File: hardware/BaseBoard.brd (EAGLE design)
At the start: 71.1 x 46.8 mm, 10 parts

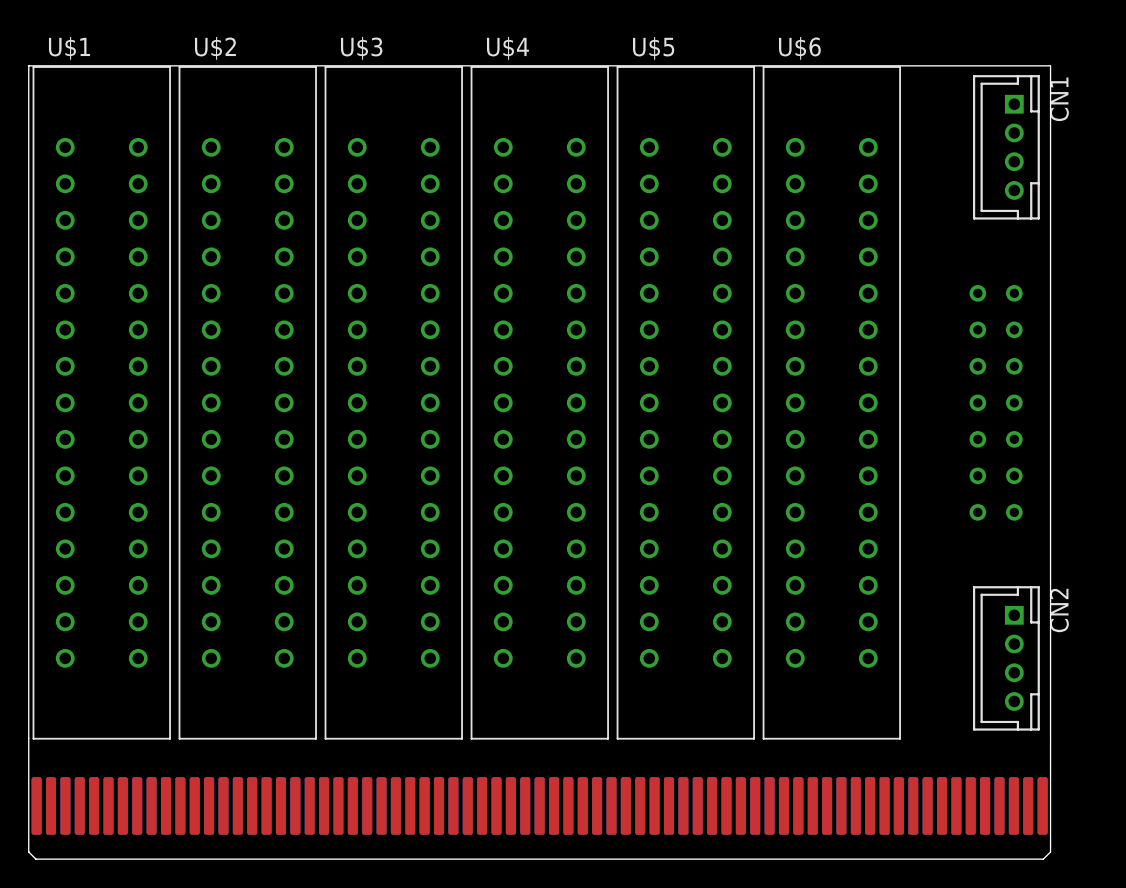
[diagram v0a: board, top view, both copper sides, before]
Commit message: Layout and route base board
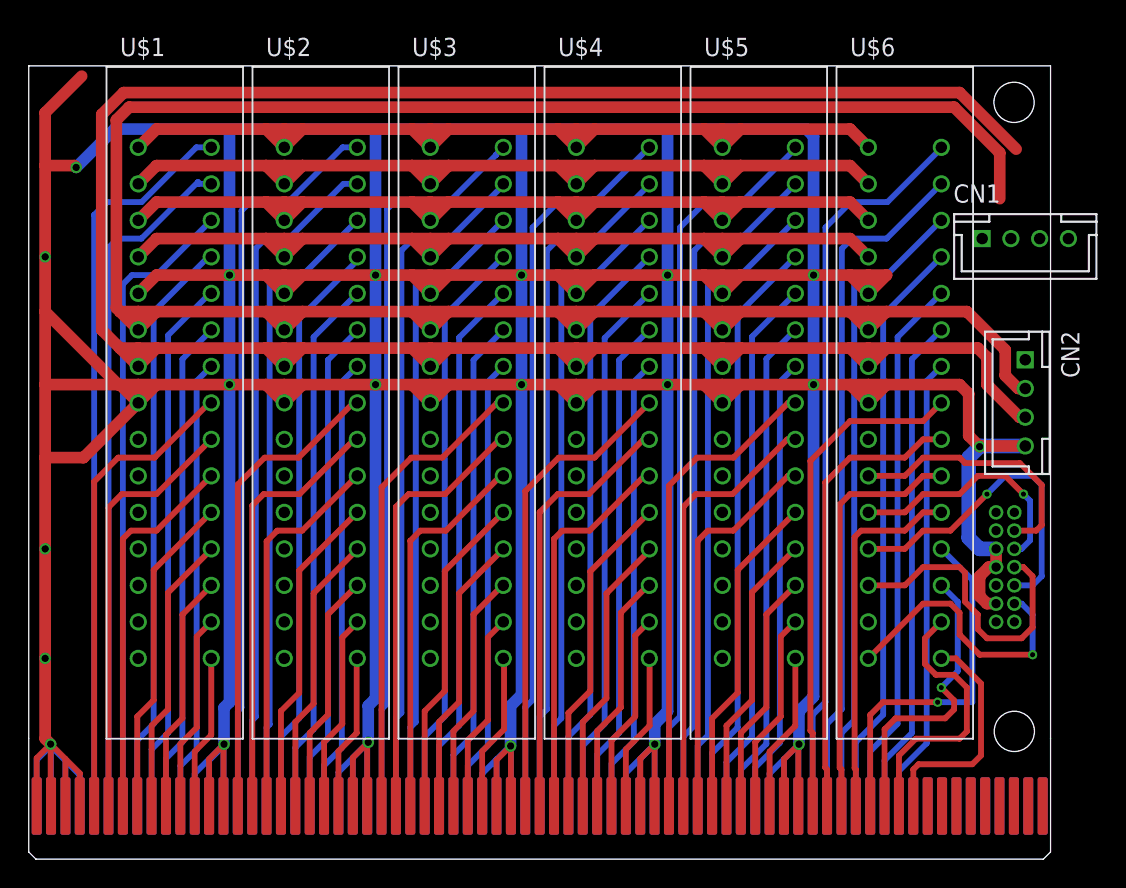
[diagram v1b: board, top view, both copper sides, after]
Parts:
- moved CN2 17.8 mm to (69.3, 31.8)
- moved U$7 11.4 mm to (67.3, 20.3)
- moved CN1 6.40 mm to (69.3, 43.2), turned to 0 degrees
- moved U$3 5.08 mm to (30.5, 31.8)
- moved U$1 5.08 mm to (10.2, 31.8)
- moved U$2 5.08 mm to (20.3, 31.8)
- moved U$4 5.08 mm to (40.6, 31.8)
- moved U$5 5.08 mm to (50.8, 31.8)
- moved U$6 5.08 mm to (61.0, 31.8)
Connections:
- new net !JNTRST!: U$6.P14
- new net !NRST!: U$6.P15, U$7.P12
- new net A01: U$1.P16, U$8.A16
- new net A02: U$1.P17, U$8.A17
- new net A03: U$1.P18, U$8.A18
- new net A04: U$1.P19, U$8.A19
- new net A05: U$1.P20, U$8.A20
- new net A06: U$1.P21, U$8.A21
- new net A07: U$1.P22, U$8.A22
- new net A08: U$1.P23, U$8.B16
- new net A09: U$1.P24, U$8.B17
- new net A10: U$1.P25, U$8.B18
- new net A11: U$1.P26, U$8.B19
- new net A12: U$1.P27, U$8.B20
- new net A13: U$1.P28, U$8.B21
- new net A14: U$1.P29, U$8.B22
- new net A15: U$1.P30, U$8.B23
- new net B01: U$2.P16, U$8.A26
- new net B02: U$2.P17, U$8.A27
- new net B03: U$2.P18, U$8.A28
- new net B04: U$2.P19, U$8.A29
- new net B05: U$2.P20, U$8.A30
- new net B06: U$2.P21, U$8.A31
- new net B07: U$2.P22, U$8.A32
- new net B08: U$2.P23, U$8.B26
- new net B09: U$2.P24, U$8.B27
- new net B10: U$2.P25, U$8.B28
- new net B11: U$2.P26, U$8.B29
- new net B12: U$2.P27, U$8.B30
- new net B13: U$2.P28, U$8.B31
- new net B14: U$2.P29, U$8.B32
- new net B15: U$2.P30, U$8.B33
- new net C01: U$3.P16, U$8.A36
- new net C02: U$3.P17, U$8.A37
- new net C03: U$3.P18, U$8.A38
- new net C04: U$3.P19, U$8.A39
- new net C05: U$3.P20, U$8.A40
- new net C06: U$3.P21, U$8.A41
- new net C07: U$3.P22, U$8.A42
- new net C08: U$3.P23, U$8.B36
- new net C09: U$3.P24, U$8.B37
- new net C10: U$3.P25, U$8.B38
- new net C11: U$3.P26, U$8.B39
- new net C12: U$3.P27, U$8.B40
- new net C13: U$3.P28, U$8.B41
- new net C14: U$3.P29, U$8.B42
- new net C15: U$3.P30, U$8.B43
- new net CANH: CN1.3, CN2.3, U$1.P7, U$2.P7, U$3.P7, U$4.P7, U$5.P7, U$6.P7
- new net CANL: CN1.2, CN2.2, U$1.P6, U$2.P6, U$3.P6, U$4.P6, U$5.P6, U$6.P6
- new net D01: U$4.P16, U$8.A46
- new net D02: U$4.P17, U$8.A47
- new net D03: U$4.P18, U$8.A48
- new net D04: U$4.P19, U$8.A49
- new net D05: U$4.P20, U$8.A50
- new net D06: U$4.P21, U$8.A51
- new net D07: U$4.P22, U$8.A52
- new net D08: U$4.P23, U$8.B46
- new net D09: U$4.P24, U$8.B47
- new net D10: U$4.P25, U$8.B48
- new net D11: U$4.P26, U$8.B49
- new net D12: U$4.P27, U$8.B50
- new net D13: U$4.P28, U$8.B51
- new net D14: U$4.P29, U$8.B52
- new net D15: U$4.P30, U$8.B53
- new net E01: U$5.P16, U$8.A56
- new net E02: U$5.P17, U$8.A57
- new net E03: U$5.P18, U$8.A58
- new net E04: U$5.P19, U$8.A59
- new net E05: U$5.P20, U$8.A60
- new net E06: U$5.P21, U$8.A61
- new net E07: U$5.P22, U$8.A62
- new net E08: U$5.P23, U$8.B56
- new net E09: U$5.P24, U$8.B57
- new net E10: U$5.P25, U$8.B58
- new net E11: U$5.P26, U$8.B59
- new net E12: U$5.P27, U$8.B60
- new net E13: U$5.P28, U$8.B61
- new net E14: U$5.P29, U$8.B62
- new net E15: U$5.P30, U$8.B63
- new net F01: U$6.P16, U$8.A66
- new net F02: U$6.P17, U$8.A67
- new net F03: U$6.P18, U$8.A68
- new net F04: U$6.P19, U$8.A69
- new net F05: U$6.P20, U$8.A70
- new net F06: U$6.P21, U$8.A71
- new net F07: U$6.P22, U$8.A72
- new net F08: U$6.P23, U$8.B66
- new net F09: U$6.P24, U$8.B67
- new net F10: U$6.P25, U$8.B68
- new net F11: U$6.P26, U$8.B69
- new net F12: U$6.P27, U$8.B70
- new net F13: U$6.P28, U$8.B71
- new net F14: U$6.P29, U$8.B72
- new net F15: U$6.P30, U$8.B73
- new net GND: CN1.4, CN2.4, U$1.P5, U$1.P8, U$2.P5, U$2.P8, U$3.P5, U$3.P8, U$4.P5, U$4.P8, U$5.P5, U$5.P8, U$6.P5, U$6.P8, U$7.P11, U$7.P5, U$7.P7, U$8.A12, U$8.A13, U$8.A14, U$8.A15, U$8.A23, U$8.A24, U$8.A25, U$8.A33, U$8.A34, U$8.A35, U$8.A43, U$8.A44, U$8.A45, U$8.A53, U$8.A54, U$8.A55, U$8.A63, U$8.A64, U$8.A65, U$8.B12, U$8.B13, U$8.B14, U$8.B15, U$8.B24, U$8.B25, U$8.B34, U$8.B35, U$8.B44, U$8.B45, U$8.B54, U$8.B55, U$8.B64, U$8.B65
- new net JCLK: U$7.P9
- new net JCLK/SWCLK: U$6.P11, U$7.P6
- new net JTDI: U$6.P12, U$7.P10
- new net JTDO/SWO: U$6.P13, U$7.P8
- new net JTMS/SWDIO: U$6.P10, U$7.P4
- new net N$11: U$1.P10
- new net N$118: U$5.P10
- new net N$119: U$5.P11
- new net N$12: U$1.P11
- new net N$120: U$5.P12
- new net N$121: U$5.P13
- new net N$122: U$5.P14
- new net N$123: U$5.P15
- new net N$13: U$1.P12
- new net N$14: U$1.P13
- new net N$15: U$1.P14
- new net N$16: U$1.P15
- new net N$180: U$8.B74
- new net N$181: U$8.B75
- new net N$191: U$8.B76
- new net N$192: U$8.B77
- new net N$193: U$8.B78
- new net N$194: U$8.B79
- new net N$195: U$8.B80
- new net N$196: U$8.B81
- new net N$197: U$8.B82
- new net N$259: U$8.A73
- new net N$260: U$8.A74
- new net N$262: U$8.A75
- new net N$263: U$8.A76
- new net N$264: U$8.A77
- new net N$265: U$8.A78
- new net N$266: U$8.A79
- new net N$267: U$8.A80
- new net N$268: U$8.A81
- new net N$269: U$8.A82
- new net N$3: U$2.P10
- new net N$4: U$2.P11
- new net N$5: U$2.P12
- new net N$6: U$2.P13
- new net N$60: U$3.P10
- new net N$61: U$3.P11
- new net N$62: U$3.P12
- new net N$63: U$3.P13
- new net N$64: U$3.P14
- new net N$65: U$3.P15
- new net N$7: U$2.P14
- new net N$8: U$2.P15
- new net N$89: U$4.P10
- new net N$90: U$4.P11
- new net N$91: U$4.P12
- new net N$92: U$4.P13
- new net N$93: U$4.P14
- new net N$94: U$4.P15
- new net T_VCC: U$7.P3
- new net VBU: U$1.P4, U$2.P4, U$3.P4, U$4.P4, U$5.P4, U$6.P4
- new net VCC: U$1.P2, U$2.P2, U$3.P2, U$4.P2, U$5.P2, U$6.P2
- new net VCP_RX: U$7.P13
- new net VCP_TX: U$7.P14
- new net VDD: U$1.P3, U$2.P3, U$3.P3, U$4.P3, U$5.P3, U$6.P3
- new net VPP: CN1.1, CN2.1, U$1.P1, U$2.P1, U$3.P1, U$4.P1, U$5.P1, U$6.P1
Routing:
- net GND: track 0.00 -> 675.8 mm, vias 0 -> 21
- net CANH: track 0.00 -> 177.9 mm
- net CANL: track 0.00 -> 175.2 mm
- net VBU: track 0.00 -> 71.3 mm
- net VDD: track 0.00 -> 71.3 mm
- net VCC: track 0.00 -> 71.3 mm
- net VPP: track 0.00 -> 71.3 mm
- net C01: track 0.00 -> 51.6 mm
- net B01: track 0.00 -> 51.4 mm
- net A01: track 0.00 -> 51.2 mm
- net F01: track 0.00 -> 51.0 mm
- net E01: track 0.00 -> 51.0 mm
- net D01: track 0.00 -> 50.9 mm
- net A02: track 0.00 -> 48.0 mm
- net F02: track 0.00 -> 48.0 mm
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
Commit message: Complete base board
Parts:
- turned CN1 to 270 degrees
- renumbered U$1 to A, U$2 to B, U$3 to C, U$4 to D, U$5 to E, U$6 to F
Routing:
- net VPP: track 71.3 -> 106.1 mm, vias 0 -> 1
- net GND: track 675.8 -> 699.6 mm, vias 21 -> 27
- net CANH: track 177.9 -> 184.8 mm
- net CANL: track 175.2 -> 178.7 mm, vias 0 -> 2
- added copper zone on layer 1, net GND
- added copper zone on layer 16, net GND

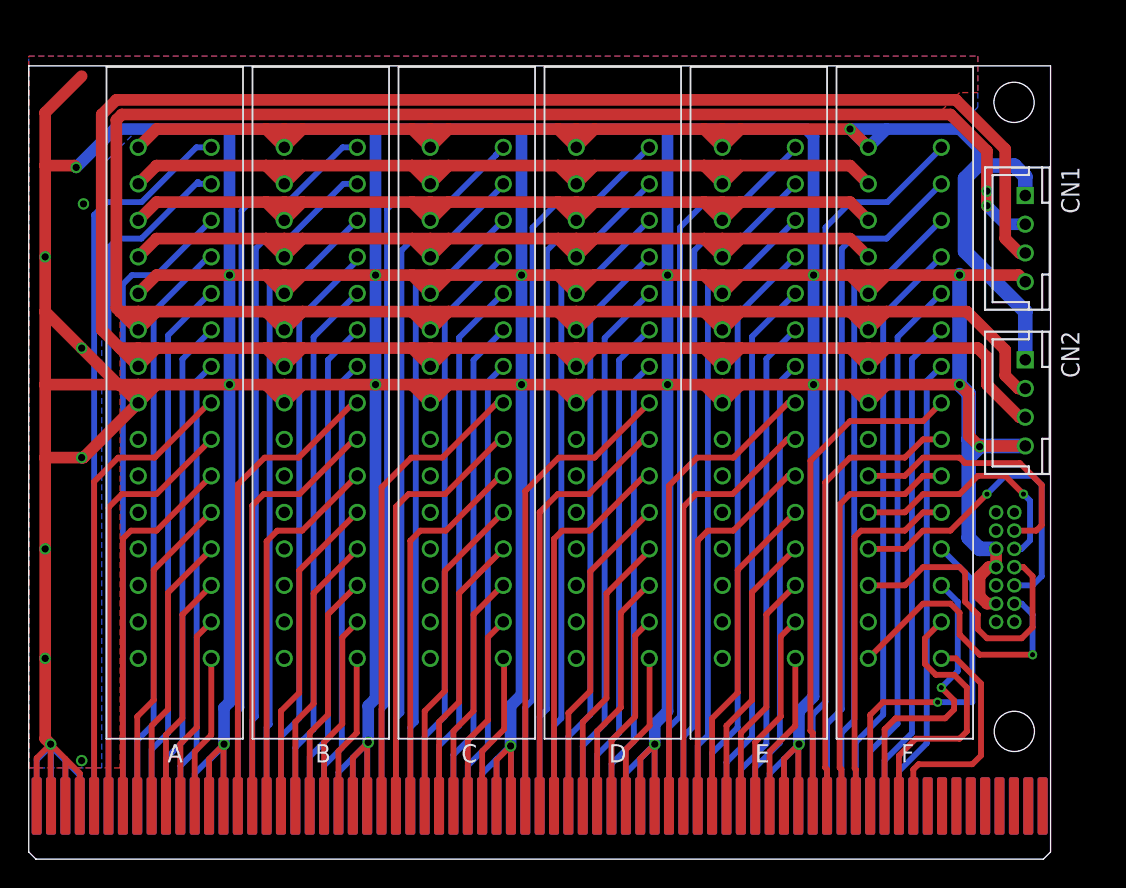
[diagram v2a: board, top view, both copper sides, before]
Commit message: Clean silk print
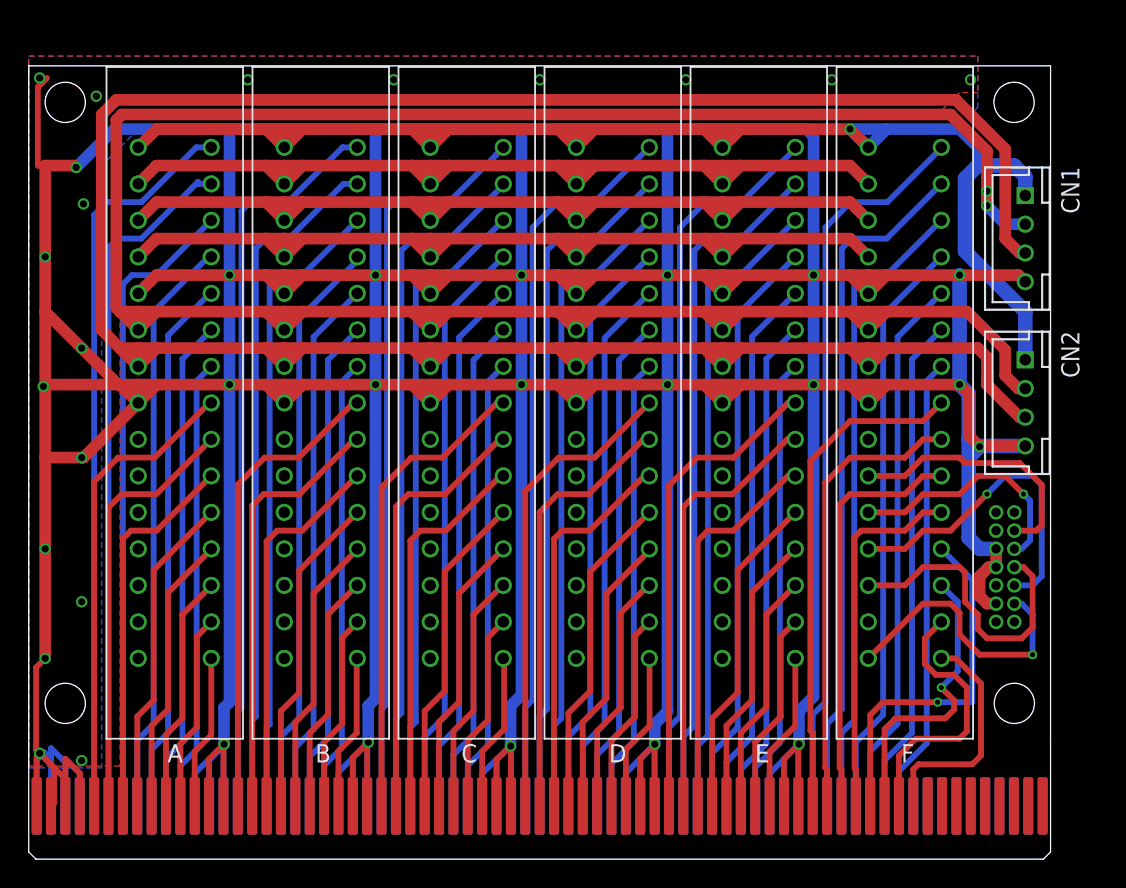
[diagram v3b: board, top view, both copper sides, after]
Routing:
- net GND: track 699.6 -> 700.3 mm, vias 27 -> 37
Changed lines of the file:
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@@
 <layer number="42" name="bRestrict" color="1" fill="10" visible="yes" active="yes"/>
 <layer number="43" name="vRestrict" color="2" fill="10" visible="no" active="yes"/>
-<layer number="44" name="Drills" color="7" fill="1" visible="no" active="yes"/>
-<layer number="45" name="Holes" color="7" fill="1" visible="no" active="yes"/>
+<layer number="44" name="Drills" color="7" fill="1" visible="yes" active="yes"/>
+<layer number="45" name="Holes" color="7" fill="1" visible="yes" active="yes"/>
 <layer number="46" name="Milling" color="3" fill="1" visible="no" active="yes"/>
 <layer number="47" name="Measures" color="7" fill="1" visible="no" active="yes"/>
@@
 <wire x1="71.1" y1="55.2" x2="71.1" y2="8.4" width="0" layer="20"/>
 <hole x="68.56" y="52.66" drill="2.8"/>
-<hole x="68.58" y="8.89" drill="2.8"/>
+<hole x="68.58" y="10.84" drill="2.8"/>
+<hole x="2.54" y="52.66" drill="2.8"/>
+<hole x="2.54" y="10.84" drill="2.8"/>
 </plain>
 <attributes>
@@
 <wire x1="13.97" y1="50.8" x2="5.969" y2="50.8" width="0.8128" layer="16"/>
 <wire x1="5.969" y1="50.8" x2="3.302" y2="48.133" width="0.8128" layer="16"/>
-<via x="1.524" y="8.001" extent="1-16" drill="0.5"/>
-<wire x1="3.55" y1="3.7" x2="3.55" y2="5.848" width="0.4064" layer="16"/>
-<wire x1="3.55" y1="5.848" x2="2.55" y2="6.848" width="0.4064" layer="16"/>
-<wire x1="1.524" y1="7.874" x2="1.524" y2="8.001" width="0.4064" layer="16"/>
-<wire x1="2.55" y1="3.7" x2="2.55" y2="6.848" width="0.4064" layer="16"/>
-<wire x1="2.55" y1="6.848" x2="1.55" y2="7.848" width="0.4064" layer="16"/>
-<wire x1="1.55" y1="3.7" x2="1.55" y2="7.848" width="0.4064" layer="16"/>
-<wire x1="1.55" y1="7.848" x2="1.524" y2="7.874" width="0.4064" layer="16"/>
+<via x="0.762" y="7.366" extent="1-16" drill="0.5"/>
+<wire x1="3.55" y1="3.7" x2="3.55" y2="5.975" width="0.4064" layer="16"/>
+<wire x1="3.55" y1="5.975" x2="2.55" y2="6.975" width="0.4064" layer="16"/>
+<wire x1="0.762" y1="7.112" x2="0.762" y2="7.366" width="0.4064" layer="16"/>
+<wire x1="2.55" y1="3.7" x2="2.55" y2="6.721" width="0.4064" layer="16"/>
+<wire x1="2.55" y1="6.721" x2="2.55" y2="6.975" width="0.4064" layer="16"/>
+<wire x1="2.55" y1="6.721" x2="1.55" y2="7.721" width="0.4064" layer="16"/>
+<wire x1="1.55" y1="6.959" x2="1.0795" y2="7.4295" width="0.4064" layer="16"/>
+<wire x1="1.55" y1="3.7" x2="1.55" y2="6.959" width="0.4064" layer="16"/>
+<wire x1="1.55" y1="6.959" x2="1.55" y2="7.721" width="0.4064" layer="16"/>
 <wire x1="0.55" y1="3.7" x2="0.55" y2="6.9" width="0.4064" layer="16"/>
-<wire x1="0.55" y1="6.9" x2="1.524" y2="7.874" width="0.4064" layer="16"/>
-<wire x1="1.55" y1="3.7" x2="1.524" y2="3.726" width="0.4064" layer="1"/>
-<wire x1="1.524" y1="3.726" x2="1.524" y2="8.001" width="0.4064" layer="1"/>
-<wire x1="0.55" y1="3.7" x2="0.55" y2="7.027" width="0.4064" layer="1"/>
-<wire x1="0.55" y1="7.027" x2="1.524" y2="8.001" width="0.4064" layer="1"/>
-<wire x1="2.55" y1="3.7" x2="2.55" y2="6.975" width="0.4064" layer="1"/>
-<wire x1="2.55" y1="6.975" x2="1.524" y2="8.001" width="0.4064" layer="1"/>
+<wire x1="0.55" y1="6.9" x2="0.762" y2="7.112" width="0.4064" layer="16"/>
+<wire x1="0.762" y1="7.112" x2="1.0795" y2="7.4295" width="0.4064" layer="16"/>
+<wire x1="1.778" y1="6.35" x2="1.778" y2="3.928" width="0.4064" layer="1"/>
+<wire x1="1.55" y1="3.7" x2="1.778" y2="3.928" width="0.4064" layer="1"/>
+<wire x1="1.778" y1="6.35" x2="0.762" y2="7.366" width="0.4064" layer="1"/>
+<wire x1="0.55" y1="3.7" x2="0.55" y2="7.154" width="0.4064" layer="1"/>
+<wire x1="0.55" y1="7.154" x2="0.762" y2="7.366" width="0.4064" layer="1"/>
+<wire x1="2.55" y1="3.7" x2="2.55" y2="5.578" width="0.4064" layer="1"/>
+<wire x1="2.55" y1="5.578" x2="2.55" y2="6.975" width="0.4064" layer="1"/>
+<wire x1="2.55" y1="5.578" x2="0.762" y2="7.366" width="0.4064" layer="1"/>
 <wire x1="3.55" y1="3.7" x2="3.55" y2="5.975" width="0.4064" layer="1"/>
 <wire x1="3.55" y1="5.975" x2="2.55" y2="6.975" width="0.4064" layer="1"/>
-<wire x1="1.524" y1="8.001" x2="1.143" y2="8.382" width="0.8128" layer="1"/>
-<wire x1="1.143" y1="8.382" x2="1.143" y2="13.97" width="0.8128" layer="1"/>
+<wire x1="0.508" y1="13.335" x2="0.508" y2="7.62" width="0.4064" layer="1"/>
+<wire x1="0.508" y1="7.62" x2="0.762" y2="7.366" width="0.4064" layer="1"/>
+<wire x1="0.508" y1="13.335" x2="1.143" y2="13.97" width="0.4064" layer="1"/>
 <wire x1="1.143" y1="13.97" x2="1.143" y2="21.59" width="0.8128" layer="1"/>
 <wire x1="1.143" y1="21.59" x2="1.143" y2="27.94" width="0.8128" layer="1"/>
@@
 <wire x1="1.143" y1="38.1" x2="1.143" y2="41.91" width="0.8128" layer="1"/>
 <wire x1="1.143" y1="41.91" x2="1.143" y2="48.26" width="0.8128" layer="1"/>
-<wire x1="1.143" y1="48.26" x2="1.143" y2="51.943" width="0.8128" layer="1"/>
-<wire x1="3.683" y1="54.483" x2="1.143" y2="51.943" width="0.8128" layer="1"/>
+<wire x1="0.635" y1="48.26" x2="0.635" y2="53.721" width="0.4064" layer="1"/>
+<wire x1="1.27" y1="54.356" x2="0.635" y2="53.721" width="0.4064" layer="1"/>
 <wire x1="7.62" y1="31.75" x2="3.81" y2="27.94" width="0.8128" layer="1"/>
 <wire x1="3.81" y1="27.94" x2="3.683" y2="27.94" width="0.8128" layer="1"/>
@@
 <wire x1="3.302" y1="48.133" x2="3.175" y2="48.26" width="0.8128" layer="1"/>
 <wire x1="3.175" y1="48.26" x2="1.143" y2="48.26" width="0.8128" layer="1"/>
+<wire x1="1.143" y1="48.26" x2="0.635" y2="48.26" width="0.4064" layer="1"/>
 <via x="1.143" y="13.97" extent="1-16" drill="0.5"/>
 <via x="1.143" y="21.59" extent="1-16" drill="0.5"/>
@@
 <wire x1="65.913" y1="28.702" x2="65.405" y2="29.21" width="1.016" layer="16"/>
 <polygon width="0" layer="1">
-<vertex x="6.35" y="6.35"/>
-<vertex x="0" y="6.35"/>
+<vertex x="6.35" y="6.477"/>
+<vertex x="0" y="6.477"/>
 <vertex x="0" y="55.88"/>
 <vertex x="66.04" y="55.88"/>
@@
 <vertex x="6.35" y="52.07"/>
 </polygon>
+<via x="3.683" y="17.907" extent="1-16" drill="0.5"/>
+<via x="1.016" y="32.893" extent="1-16" drill="0.5"/>
+<via x="0.762" y="54.356" extent="1-16" drill="0.5"/>
+<via x="4.699" y="53.086" extent="1-16" drill="0.5"/>
+<via x="15.24" y="54.229" extent="1-16" drill="0.5"/>
+<via x="25.4" y="54.229" extent="1-16" drill="0.5"/>
+<via x="35.56" y="54.229" extent="1-16" drill="0.5"/>
+<via x="45.72" y="54.229" extent="1-16" drill="0.5"/>
+<via x="55.88" y="54.229" extent="1-16" drill="0.5"/>
+<via x="65.532" y="54.229" extent="1-16" drill="0.5"/>
 </signal>
 <signal name="CANL">
